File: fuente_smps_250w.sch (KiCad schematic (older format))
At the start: 12 parts, among them J1 Conn_01x03, J2 Conn_01x03, U2 LTV-817S-TA1

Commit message: terminando la  version con sg3525a
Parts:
- H1, H2, H3, H4: symbol Mechanical:MountingHole_Pad -> fuente_smps_250w-rescue:MountingHole_Pad-Mechanical
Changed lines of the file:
@@
 	5700 2950 5700 2300
 $Comp
-L Mechanical:MountingHole_Pad H3
+L fuente_smps_250w-rescue:MountingHole_Pad-Mechanical H3
 U 1 1 5F985F1B
 P 6600 5750
@@
 	6600 5900 6600 5850
 $Comp
-L Mechanical:MountingHole_Pad H4
+L fuente_smps_250w-rescue:MountingHole_Pad-Mechanical H4
 U 1 1 5F987739
 P 6900 5750
@@
 	6900 5900 6900 5850
 $Comp
-L Mechanical:MountingHole_Pad H1
+L fuente_smps_250w-rescue:MountingHole_Pad-Mechanical H1
 U 1 1 5F988874
 P 3650 5750
@@
 	3650 5900 3650 5850
 $Comp
-L Mechanical:MountingHole_Pad H2
+L fuente_smps_250w-rescue:MountingHole_Pad-Mechanical H2
 U 1 1 5F98888A
 P 3950 5750

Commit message: terminando el diseno
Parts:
- renumbered D3 to D1, D4 to D2, R13 to R1, R14 to R2, U2 to U1
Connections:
- net GND: no longer H1.1, H2.1
- net GNDREF: no longer H3.1, H4.1
- net OSC_SG3525/Sense renamed OSC_TL494/Sense
- net OSC_SG3525/VREF renamed OSC_TL494/VREF
- net OSC_SG3525/shutdown renamed OSC_TL494/shutdown
- no-connect marks 0 -> 4
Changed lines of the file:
@@
 Rev "V 0.1.0"
 Comp "PCB PROFESIONAL"
-Comment1 ""
+Comment1 "https://maykolrey.com"
 Comment2 ""
 Comment3 ""
@@
 S 3800 2650 950  750
 U 5F9067C9
-F0 "OSC_SG3525" 50
-F1 "OSC_SG3525.sch" 50
+F0 "OSC_TL494" 50
+F1 "OSC_TL494.sch" 50
 F2 "Sense" I L 3800 3200 50
 F3 "shutdown" O L 3800 2800 50
@@
 $EndComp
 $Comp
-L power:+12V #PWR06
+L power:+12V #PWR01
 U 1 1 5F934619
 P 3450 2600
-F 0 "#PWR06" H 3450 2450 50  0001 C CNN
+F 0 "#PWR01" H 3450 2450 50  0001 C CNN
 F 1 "+12V" H 3465 2773 50  0000 C CNN
 F 2 "" H 3450 2600 50  0001 C CNN
@@
 	3450 2700 3350 2700
 $Comp
-L power:GND #PWR07
+L power:GND #PWR02
 U 1 1 5F934E96
 P 3450 2950
-F 0 "#PWR07" H 3450 2700 50  0001 C CNN
+F 0 "#PWR02" H 3450 2700 50  0001 C CNN
 F 1 "GND" H 3455 2777 50  0000 C CNN
 F 2 "" H 3450 2950 50  0001 C CNN
@@
 	3350 2800 3800 2800
 $Comp
-L MSS_Optocopler:LTV-817S-TA1 U2
+L MSS_Optocopler:LTV-817S-TA1 U1
 U 1 1 5F92E8F7
 P 5700 4850
-F 0 "U2" H 5900 5050 50  0000 C CNN
+F 0 "U1" H 5900 5050 50  0000 C CNN
 F 1 "LTV-817S-TA1" H 5725 5084 50  0001 C CNN
 F 2 "Package_DIP:DIP-4_W7.62mm_LongPads" H 5650 4850 50  0001 C CNN
@@
 $EndComp
 $Comp
-L Device:D_Zener_ALT D3
+L Device:D_Zener_ALT D1
 U 1 1 5F9317CF
 P 6850 4750
-F 0 "D3" H 6850 4533 50  0000 C CNN
+F 0 "D1" H 6850 4533 50  0000 C CNN
 F 1 "D_Zener_ALT" H 6850 4624 50  0000 C CNN
 F 2 "Diode_THT:D_A-405_P10.16mm_Horizontal" H 6850 4750 50  0001 C CNN
@@
 $EndComp
 $Comp
-L Device:D_Zener_ALT D4
+L Device:D_Zener_ALT D2
 U 1 1 5F93291B
 P 7450 4750
-F 0 "D4" H 7450 4533 50  0000 C CNN
+F 0 "D2" H 7450 4533 50  0000 C CNN
 F 1 "D_Zener_ALT" H 7450 4624 50  0000 C CNN
 F 2 "Diode_THT:D_A-405_P10.16mm_Horizontal" H 7450 4750 50  0001 C CNN
@@
 	7000 4750 7300 4750
 $Comp
-L Device:R R14
+L Device:R R2
 U 1 1 5F933DFD
 P 7150 4950
-F 0 "R14" V 7265 4950 50  0000 C CNN
+F 0 "R2" V 7265 4950 50  0000 C CNN
 F 1 "510" V 7356 4950 50  0000 C CNN
 F 2 "Resistor_THT:R_Axial_DIN0207_L6.3mm_D2.5mm_P10.16mm_Horizontal" V 7080 4950 50  0001 C CNN
@@
 	3650 4750 5250 4750
 $Comp
-L Device:R R13
+L Device:R R1
 U 1 1 5F93E75F
 P 5200 5200
-F 0 "R13" H 5130 5154 50  0000 R CNN
+F 0 "R1" H 5130 5154 50  0000 R CNN
 F 1 "1K" H 5130 5245 50  0000 R CNN
 F 2 "Resistor_THT:R_Axial_DIN0207_L6.3mm_D2.5mm_P10.16mm_Horizontal" V 5130 5200 50  0001 C CNN
@@
 	5200 4950 5200 5050
 $Comp
-L power:GND #PWR0101
+L power:GND #PWR05
 U 1 1 5F93F532
 P 5200 5400
-F 0 "#PWR0101" H 5200 5150 50  0001 C CNN
+F 0 "#PWR05" H 5200 5150 50  0001 C CNN
 F 1 "GND" H 5205 5227 50  0000 C CNN
 F 2 "" H 5200 5400 50  0001 C CNN
@@
 	1    0    0    -1
 $EndComp
-Wire Wire Line
-	6600 5900 6600 5850
 $Comp
 L fuente_smps_250w-rescue:MountingHole_Pad-Mechanical H4
@@
 	1    0    0    -1
 $EndComp
-Wire Wire Line
-	6900 5900 6900 5850
 $Comp
 L fuente_smps_250w-rescue:MountingHole_Pad-Mechanical H1
@@
 $EndComp
 $Comp
-L power:GND #PWR022
-U 1 1 5F98887E
-P 3650 5900
-F 0 "#PWR022" H 3650 5650 50  0001 C CNN
-F 1 "GND" H 3655 5727 50  0000 C CNN
-F 2 "" H 3650 5900 50  0001 C CNN
-F 3 "" H 3650 5900 50  0001 C CNN
-	1    3650 5900
-	1    0    0    -1
-$EndComp
-Wire Wire Line
-	3650 5900 3650 5850
-$Comp
 L fuente_smps_250w-rescue:MountingHole_Pad-Mechanical H2
 U 1 1 5F98888A
@@
 	1    0    0    -1
 $EndComp
-$Comp
-L power:GND #PWR023
-U 1 1 5F988894
-P 3950 5900
-F 0 "#PWR023" H 3950 5650 50  0001 C CNN
-F 1 "GND" H 3955 5727 50  0000 C CNN
-F 2 "" H 3950 5900 50  0001 C CNN
-F 3 "" H 3950 5900 50  0001 C CNN
-	1    3950 5900
-	1    0    0    -1
-$EndComp
-Wire Wire Line
-	3950 5900 3950 5850
-$Comp
-L power:GNDREF #PWR0102
-U 1 1 5F996AFA
-P 6900 5900
-F 0 "#PWR0102" H 6900 5650 50  0001 C CNN
-F 1 "GNDREF" H 6905 5727 50  0000 C CNN
-F 2 "" H 6900 5900 50  0001 C CNN
-F 3 "" H 6900 5900 50  0001 C CNN
-	1    6900 5900
-	1    0    0    -1
-$EndComp
-$Comp
-L power:GNDREF #PWR0103
-U 1 1 5F99893C
-P 6600 5900
-F 0 "#PWR0103" H 6600 5650 50  0001 C CNN
-F 1 "GNDREF" H 6605 5727 50  0000 C CNN
-F 2 "" H 6600 5900 50  0001 C CNN
-F 3 "" H 6600 5900 50  0001 C CNN
-	1    6600 5900
-	1    0    0    -1
-$EndComp
+NoConn ~ 3650 5850
+NoConn ~ 3950 5850
+NoConn ~ 6600 5850
+NoConn ~ 6900 5850
 $EndSCHEMATC

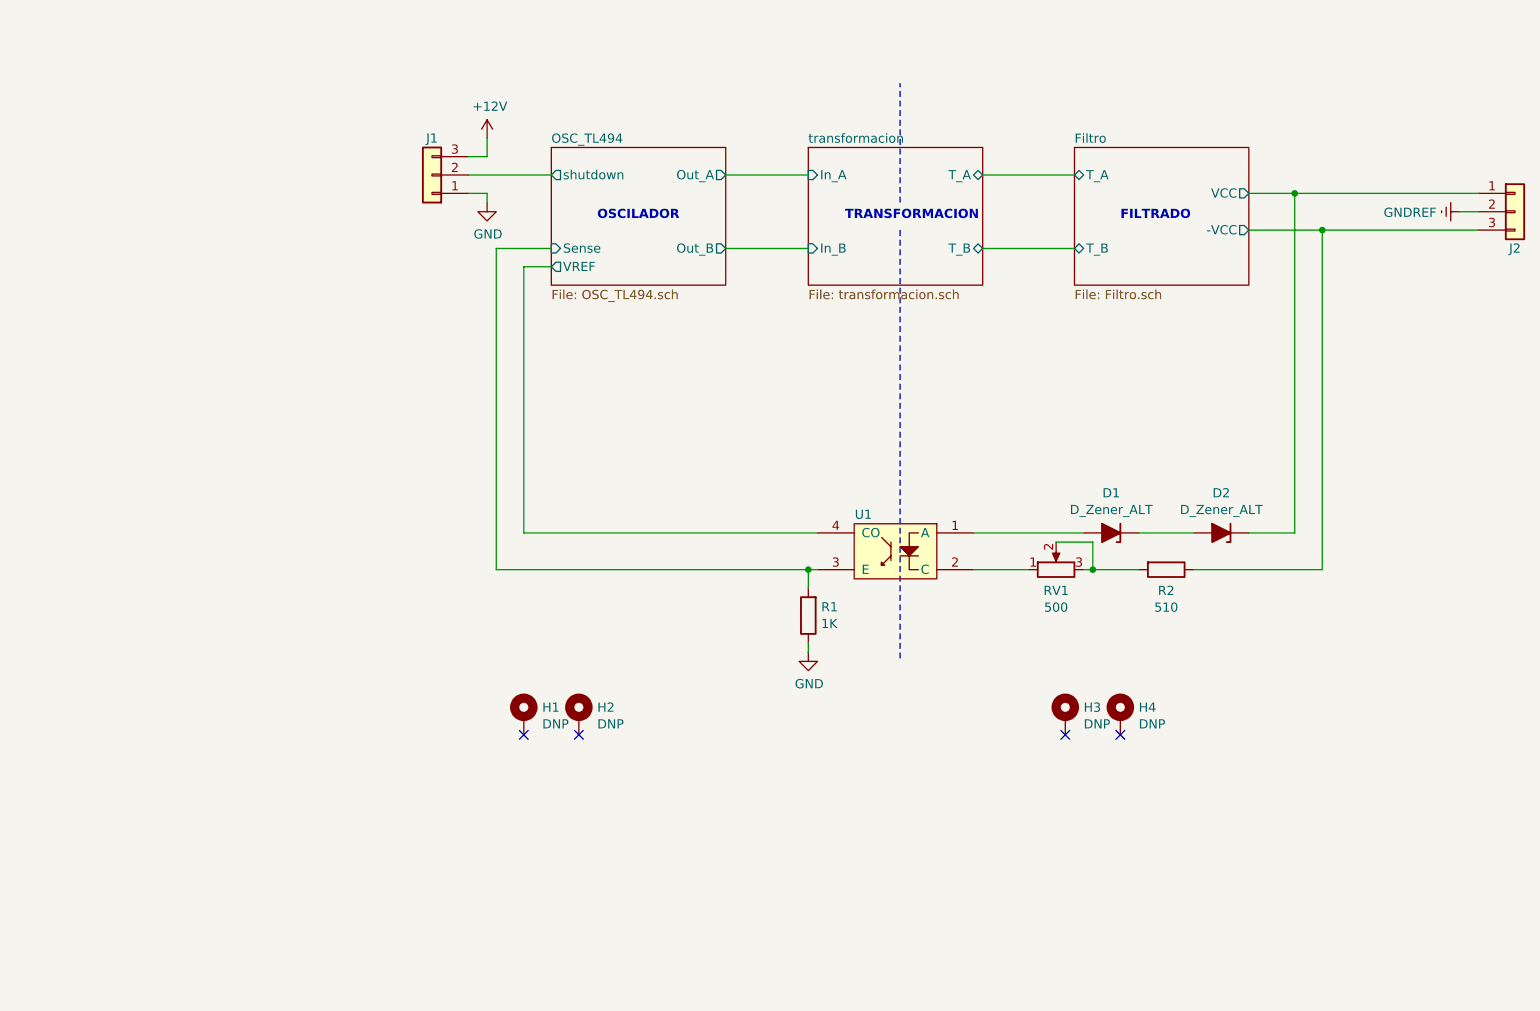
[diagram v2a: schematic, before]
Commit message: separando el modulo de oscilacion en otra  placa
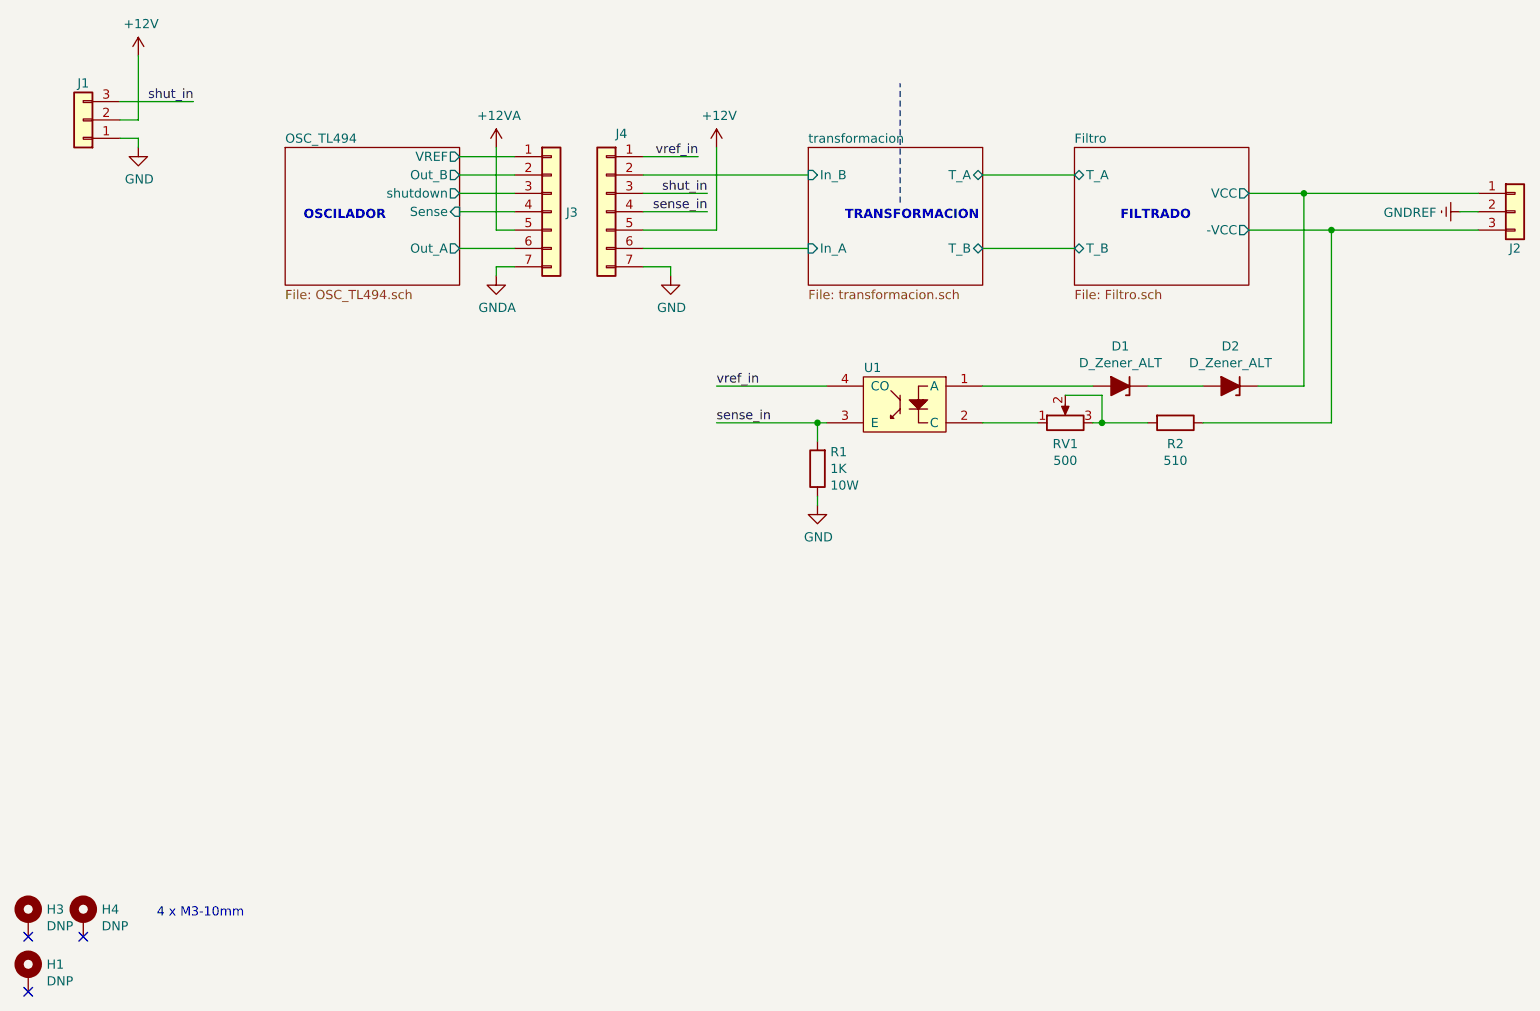
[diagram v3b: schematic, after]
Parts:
- removed H2: MountingHole_Pad, MountingHole:MountingHole_3.2mm_M3_Pad_Via, symbol fuente_smps_250w-rescue:MountingHole_Pad-Mechanical
- added J3: Conn_01x03, Connector_PinHeader_2.54mm:PinHeader_1x07_P2.54mm_Horizontal, symbol Connector_Generic:Conn_01x07
- added J4: Conn_01x03, Connector_PinSocket_2.54mm:PinSocket_1x07_P2.54mm_Vertical, symbol Connector_Generic:Conn_01x07
- R1: P (none) -> 10W
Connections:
- net +12V: now also J1.2 (Pin_2), J4.5 (Pin_5); no longer J1.3 (Pin_3)
- net GND: now also J4.7 (Pin_7)
- net OSC_TL494/Out_A: now also J3.6 (Pin_6)
- net OSC_TL494/Out_B: now also J3.2 (Pin_2)
- net OSC_TL494/Sense: now also J3.4 (Pin_4); no longer R1.2, U1.3 (E)
- net OSC_TL494/VREF: now also J3.1 (Pin_1); no longer U1.4 (CO)
- net OSC_TL494/shutdown: now also J3.3 (Pin_3); no longer J1.2 (Pin_2)
- new net +12VA: J3.5 (Pin_5)
- new net GNDA: J3.7 (Pin_7)
- new net sense_in: J4.4 (Pin_4), R1.2, U1.3 (E)
- new net shut_in: J1.3 (Pin_3), J4.3 (Pin_3)
- new net transformacion/In_A: J4.6 (Pin_6)
- new net transformacion/In_B: J4.2 (Pin_2)
- new net vref_in: J4.1 (Pin_1), U1.4 (CO)
- no-connect marks 4 -> 3
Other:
- note added: "4 x M3-10mm"
- moved on the sheet: D1, D2, H1, H3, H4, J1, R1, R2, RV1, U1
